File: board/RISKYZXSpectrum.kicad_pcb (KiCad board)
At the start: 4 copper layers, 76.9 x 87.4 mm, 31 parts, among them J1 Conn_01x02, J2 Conn_01x02, J3 Conn_02x28_Odd_Even, J4 Conn_02x28_Odd_Even, J7 USB_1, J8 Conn_01x02, SW1 SW_SPST, SW2 SW_SPST, U1 CH32V307VCT6, U2 LM1117MP-3.3

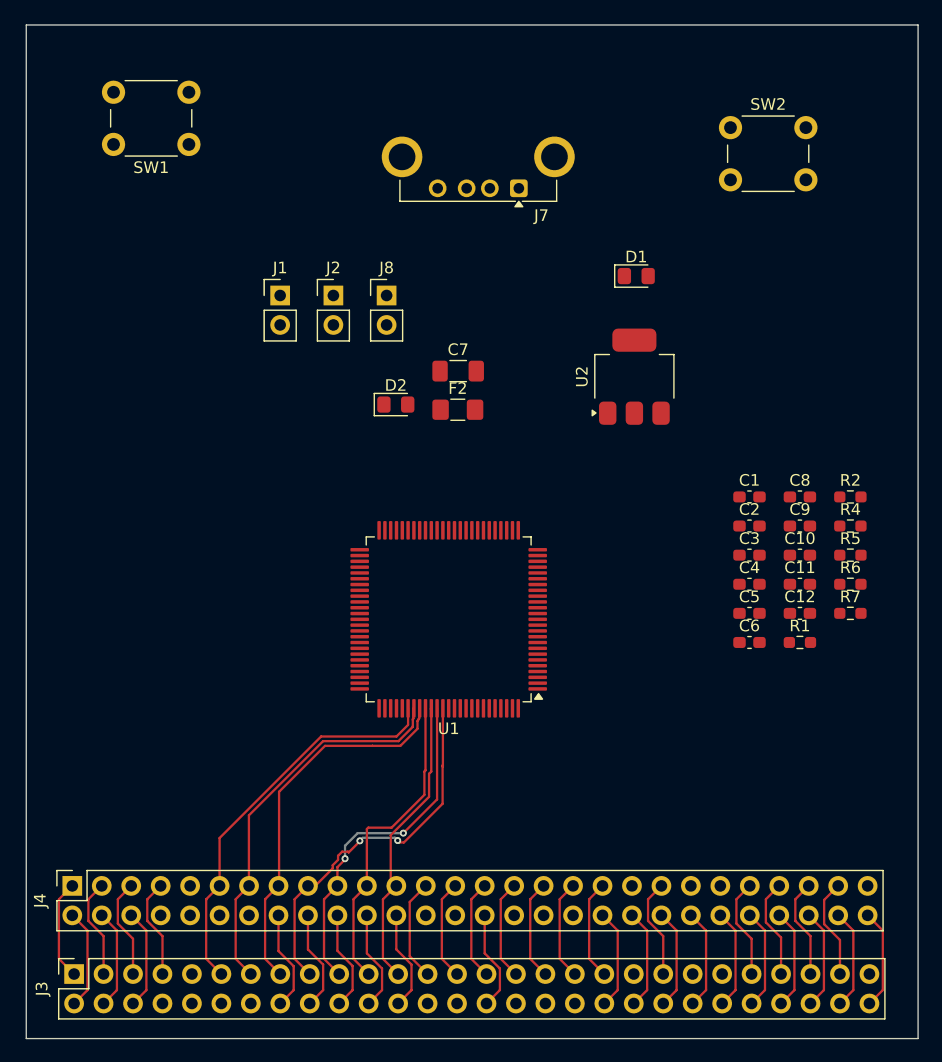
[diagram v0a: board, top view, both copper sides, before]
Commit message: Initial working device as EPROM with random game
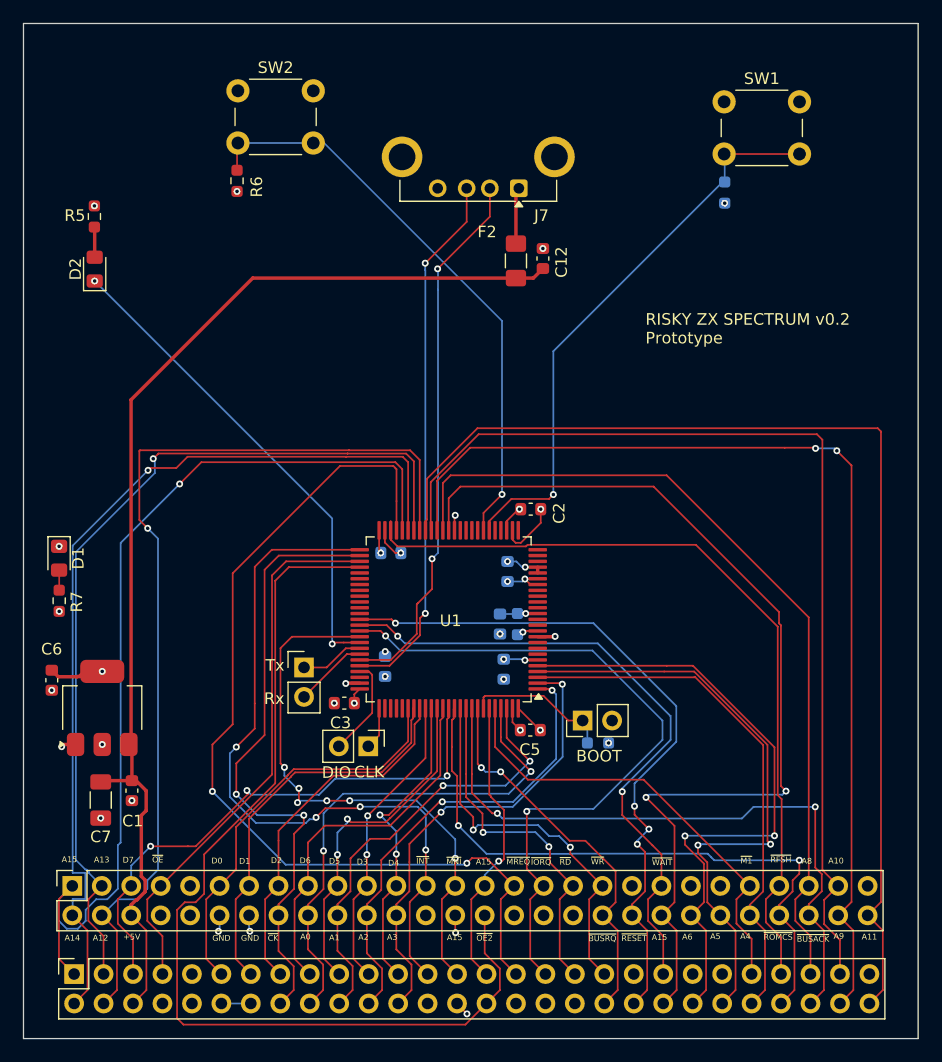
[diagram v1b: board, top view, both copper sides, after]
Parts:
- C10, C11, C4, C8, C9, R1, R2, R4: moved to B.Cu
- moved R5 71.4 mm to (101.2, 73.3), turned to 90 degrees
- moved R7 68.2 mm to (98.1, 106.5), turned to 90 degrees
- moved R6 63.3 mm to (113.5, 70.2), turned to -90 degrees
- moved C6 60.3 mm to (97.5, 113.3), turned to -90 degrees
- moved C1 59.0 mm to (104.4, 122.8), turned to -90 degrees
- moved D1 55.4 mm to (98.1, 102.8), turned to -90 degrees
- moved U2 54.1 mm to (101.8, 115.7)
- moved C7 48.1 mm to (101.7, 123.6), turned to -90 degrees
- moved SW1 46.3 mm to (155.5, 63.4), turned to 0 degrees
- moved J1 45.0 mm to (143.3, 116.8), turned to 90 degrees
- moved SW2 42.6 mm to (113.5, 62.5)
- moved J8 38.9 mm to (124.8, 119.0), turned to -90 degrees
- moved C12 37.8 mm to (139.8, 76.9), turned to 90 degrees
- moved C3 37.2 mm to (122.7, 115.3), turned to 180 degrees
- moved C10 35.3 mm to (126.7, 102.3)
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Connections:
- J3 pad 30: /~{OE} -> /~{OE2}
- J4 pad 30: /~{OE} -> /~{OE2}
- U1 pad 53: unconnected-(U1-PB14(FT)-Pad53) -> /~{OE}
- U1 pad 54: unconnected-(U1-PB15(FT)-Pad54) -> /~{OE2}
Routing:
- net +5V: track 8.62 -> 97.6 mm
- net /A11: track 8.62 -> 96.4 mm
- net /~{OE2}: track 0.00 -> 85.8 mm
- net /A9: track 8.62 -> 89.7 mm, vias 0 -> 2
- net /A10: track 8.67 -> 87.6 mm
- net /A7: track 8.62 -> 84.6 mm, vias 0 -> 2
- net /A12: track 8.62 -> 82.9 mm, vias 0 -> 1
- net /A15: track 8.62 -> 82.1 mm, vias 0 -> 1
- net /~{MREQ}: track 8.62 -> 81.4 mm, vias 0 -> 2
- net /A14: track 8.62 -> 80.9 mm, vias 0 -> 1
- net /A13: track 8.62 -> 78.2 mm, vias 0 -> 1
- net /A8: track 8.62 -> 72.7 mm
- net /~{RFSH}: track 8.62 -> 69.4 mm
- net /~{INT}: track 8.81 -> 64.0 mm, vias 0 -> 4
- net /~{IORQ}: track 8.62 -> 60.9 mm, vias 0 -> 2
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- added copper zone on In2.Cu, net +3.3V
- added copper zone on In1.Cu, net GND
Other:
- board size 76.9 x 87.4 mm -> 77.1 x 87.5 mm
- board text added: "+5V"
- board text added: "A0"
- board text added: "A1"
- board text added: "A10"
- board text added: "A11"
- board text added: "A12"
- board text added: "A13"
- board text added: "A14"
- board text added: "A15"
- board text added: "A2"
- board text added: "A3"
- board text added: "A4"
- board text added: "A5"
- board text added: "A6"
- board text added: "A8"
- board text added: "A9"
- board text added: "BOOT"
- board text added: "CLK"
- board text added: "D0"
- board text added: "D1"
- board text added: "D2"
- board text added: "D3"
- board text added: "D4"
- board text added: "D5"
- board text added: "D6"
- board text added: "D7"
- board text added: "DIO"
- board text added: "GND"
- board text added: "RISKY ZX SPECTRUM v0.2 Prototype"
- board text added: "Rx"
- board text added: "Tx"
- board text added: "~{BUSACK}"
- board text added: "~{BUSRQ}"
- board text added: "~{CK}"
- board text added: "~{INT}"
- board text added: "~{IORQ}"
- board text added: "~{M1}"
- board text added: "~{MNI}"
- board text added: "~{MREQ}"
- board text added: "~{OE2}"
- board text added: "~{OE}"
- board text added: "~{RD}"
- board text added: "~{RESET}"
- board text added: "~{RFSH}"
- board text added: "~{ROMCS}"
- board text added: "~{WAIT}"
- board text added: "~{WR}"

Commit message: PCB udpate
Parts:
- removed J3: Conn_02x28_Odd_Even, Connector_PinSocket_2.54mm:PinSocket_2x28_P2.54mm_Vertical
- removed R2: R, Resistor_SMD:R_0603_1608Metric_Pad0.98x0.95mm_HandSolder
- removed the SW1 at (155.5, 63.4)
- J4: footprint Connector_PinSocket_2.54mm:PinSocket_2x28_P2.54mm_Vertical -> edgeconnector:EdgeConnector_254x508x2x28_OddEven
- moved J4 34.3 mm to (133.5, 133.6), turned to 0 degrees
- moved SW1 25.4 mm to (107.2, 87.0)
- moved D2 22.6 mm to (121.5, 87.7)
- moved R5 22.4 mm to (118.5, 87.6), turned to -90 degrees
- moved R6 22.4 mm to (104.5, 90.8), turned to 90 degrees
- moved J7 18.0 mm to (137.7, 88.8)
- moved C12 16.4 mm to (139.8, 93.4)
- moved F2 16.4 mm to (137.5, 93.6)
- moved C11 0.25 mm to (136.5, 112.6)
- renumbered SW2 to SW1
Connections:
- R6 pad 1: /BTN2 -> /BTN1
- SW1 pad 2: /BTN2 -> /BTN1
- U1 pad 31: /BTN1 -> unconnected-(U1-PA6/ADC6-Pad31)
- U1 pad 32: /BTN2 -> /BTN1
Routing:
- net /BTN2: track 50.2 -> 0.00 mm, vias 1 -> 0
- net /A15: track 82.1 -> 48.3 mm, vias 1 -> 2
- net /A11: track 96.4 -> 65.3 mm
- net /A12: track 82.9 -> 53.0 mm
- net /A13: track 78.2 -> 48.4 mm
- net /A10: track 87.6 -> 58.1 mm
- net +5V: track 97.6 -> 69.2 mm
- net /A14: track 80.9 -> 53.2 mm, vias 1 -> 2
- net /A9: track 89.7 -> 63.7 mm
- net /~{OE2}: track 85.8 -> 62.3 mm, vias 0 -> 1
- net /~{MREQ}: track 81.4 -> 59.5 mm, vias 2 -> 1
- net /LEDFLASH: track 42.2 -> 24.0 mm
- net /USB1_DM: track 46.9 -> 28.9 mm, vias 2 -> 1
- net /USB1_DP: track 46.5 -> 28.5 mm, vias 2 -> 1
- net /A8: track 72.7 -> 55.2 mm
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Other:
- board size 77.1 x 87.5 mm -> 77.1 x 56.5 mm
- board text added: "PLAY / RESET"
- board text added: "POWER"
- board text added: "READY"
- board text added: "RISKY Speccy v1.0 Prototype"
- board text removed: "+5V"
- board text removed: "A0"
- board text removed: "A1"
- board text removed: "A10"
- board text removed: "A11"
- board text removed: "A12"
- board text removed: "A13"
- board text removed: "A14"
- board text removed: "A15"
- board text removed: "A2"
- board text removed: "A3"
- board text removed: "A4"
- board text removed: "A5"
- board text removed: "A6"
- board text removed: "A8"
- board text removed: "A9"
- board text removed: "D0"
- board text removed: "D1"
- board text removed: "D2"
- board text removed: "D3"
- board text removed: "D4"
- board text removed: "D5"
- board text removed: "D6"
- board text removed: "D7"
- board text removed: "GND"
- board text removed: "RISKY ZX SPECTRUM v0.2 Prototype"
- board text removed: "~{BUSACK}"
- board text removed: "~{BUSRQ}"
- board text removed: "~{CK}"
- board text removed: "~{INT}"
- board text removed: "~{IORQ}"
- board text removed: "~{M1}"
- board text removed: "~{MNI}"
- board text removed: "~{MREQ}"
- board text removed: "~{OE2}"
- board text removed: "~{OE}"
- board text removed: "~{RD}"
- board text removed: "~{RESET}"
- board text removed: "~{RFSH}"
- board text removed: "~{ROMCS}"
- board text removed: "~{WAIT}"
- board text removed: "~{WR}"

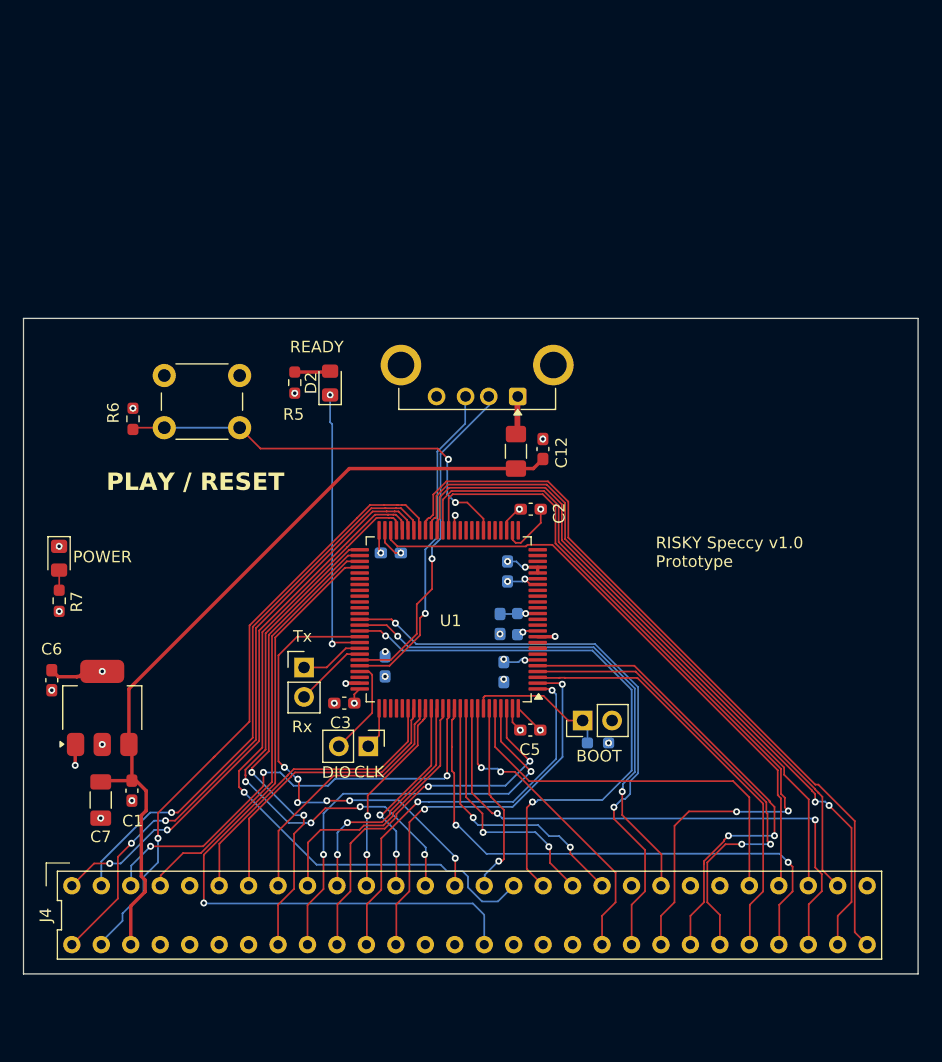
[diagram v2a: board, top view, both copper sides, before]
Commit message: Update PCB job file and firmware for ROMCS handling - Updated the PCB job file version from 10.0.1 to 10.0.3 and adjusted the creation date. - Modified the RunCartWithRAM function to configure GPIO settings for external bus control. - Enhanced the ZX_RomcsRelease and ZX_RomcsAssert functions to ensure proper handling of ROMCS and external bus OE drivers.
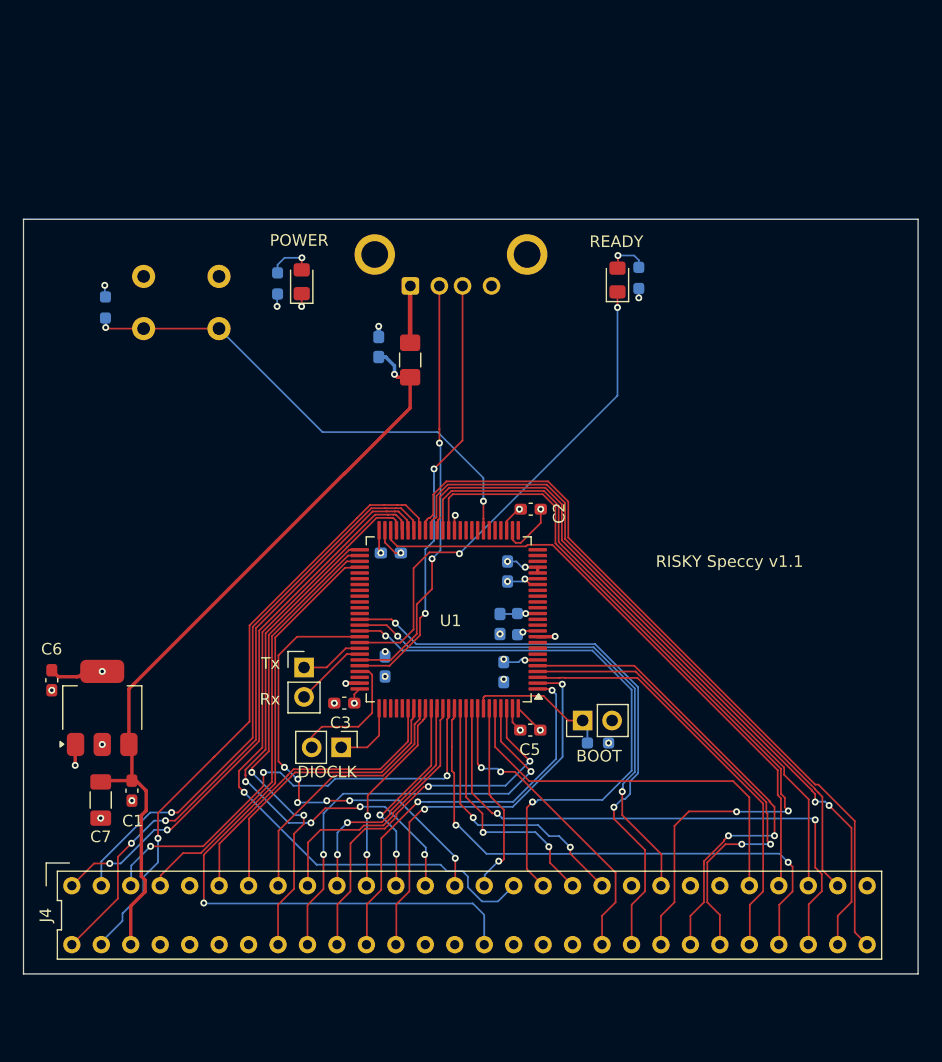
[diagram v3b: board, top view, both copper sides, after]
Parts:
- C12, J7, R5, R6, R7, SW1: moved to B.Cu
- moved R7 33.2 mm to (117.0, 79.1)
- moved D1 31.7 mm to (119.0, 78.9), turned to 90 degrees
- moved R5 31.0 mm to (148.1, 78.6)
- moved D2 26.3 mm to (146.3, 78.8)
- moved C12 16.7 mm to (125.7, 84.6)
- moved J7 13.3 mm to (128.4, 79.3), turned to 0 degrees
- moved F2 12.1 mm to (128.4, 85.7)
- moved R6 9.89 mm to (102.1, 81.2)
- moved SW1 9.76 mm to (111.9, 78.5), turned to 180 degrees
- moved J8 2.34 mm to (122.5, 119.1)
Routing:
- net /LEDFLASH: track 24.0 -> 43.2 mm
- net /USB1_DP: track 28.5 -> 38.0 mm, vias 1 -> 2
- net /USB1_DM: track 28.9 -> 36.7 mm, vias 1 -> 2
- net /BTN1: track 36.2 -> 43.3 mm
- net +5V: track 69.2 -> 66.1 mm, vias 0 -> 1
- net GND: track 19.4 -> 22.5 mm
- net /SWDIO: track 8.56 -> 11.5 mm
- net Net-(J7-VBUS): track 2.39 -> 4.91 mm
- net /SWCLK: track 3.66 -> 6.03 mm
- net Net-(D1-A): track 1.72 -> 4.09 mm, vias 0 -> 1
- net +3.3V: track 19.6 -> 21.5 mm
- net Net-(D2-A): track 2.97 -> 3.68 mm, vias 0 -> 1
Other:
- board size 77.1 x 56.5 mm -> 77.1 x 65.1 mm
- board text added: "RISKY Speccy v1.1"
- board text added: "USB"
- board text removed: "RISKY Speccy v1.0 Prototype"
